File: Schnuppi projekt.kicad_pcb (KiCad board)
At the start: 2 copper layers, 23 parts, among them Q1 BC817, Q2 BC817, SW1 SW_Push, SW2 SW_Push, SW3 SW_Push, SW4 SW_Push, SW5 SW_Push, SW6 SW_Push, U13 ESP32-WROOM-32E, U14 DM-OLED096-636, U2 TPS62065DSGR, U5 WE-TVS-82400102, U6 CH340C

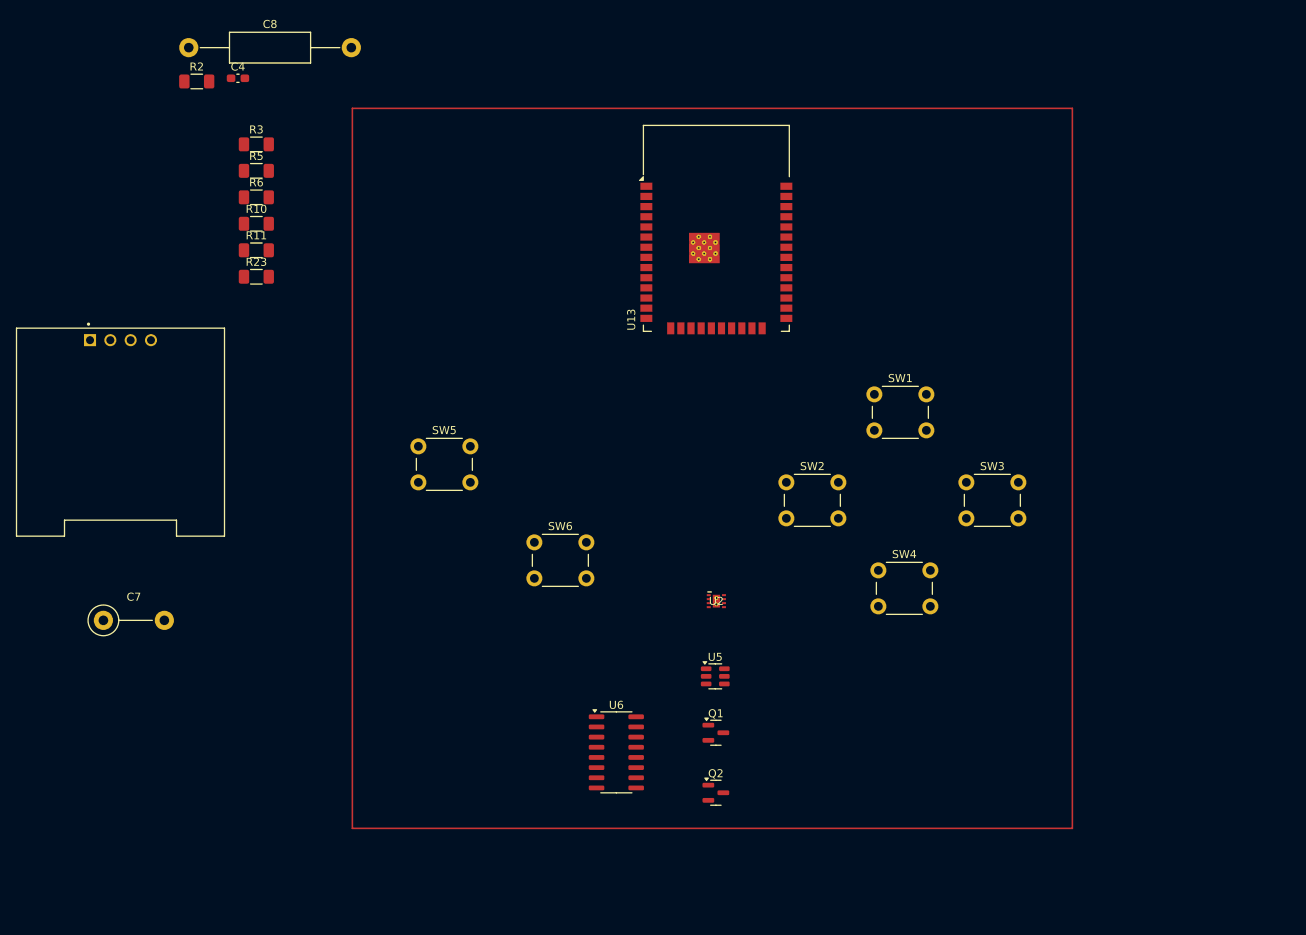
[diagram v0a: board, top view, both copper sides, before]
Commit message: added footprints for resistors
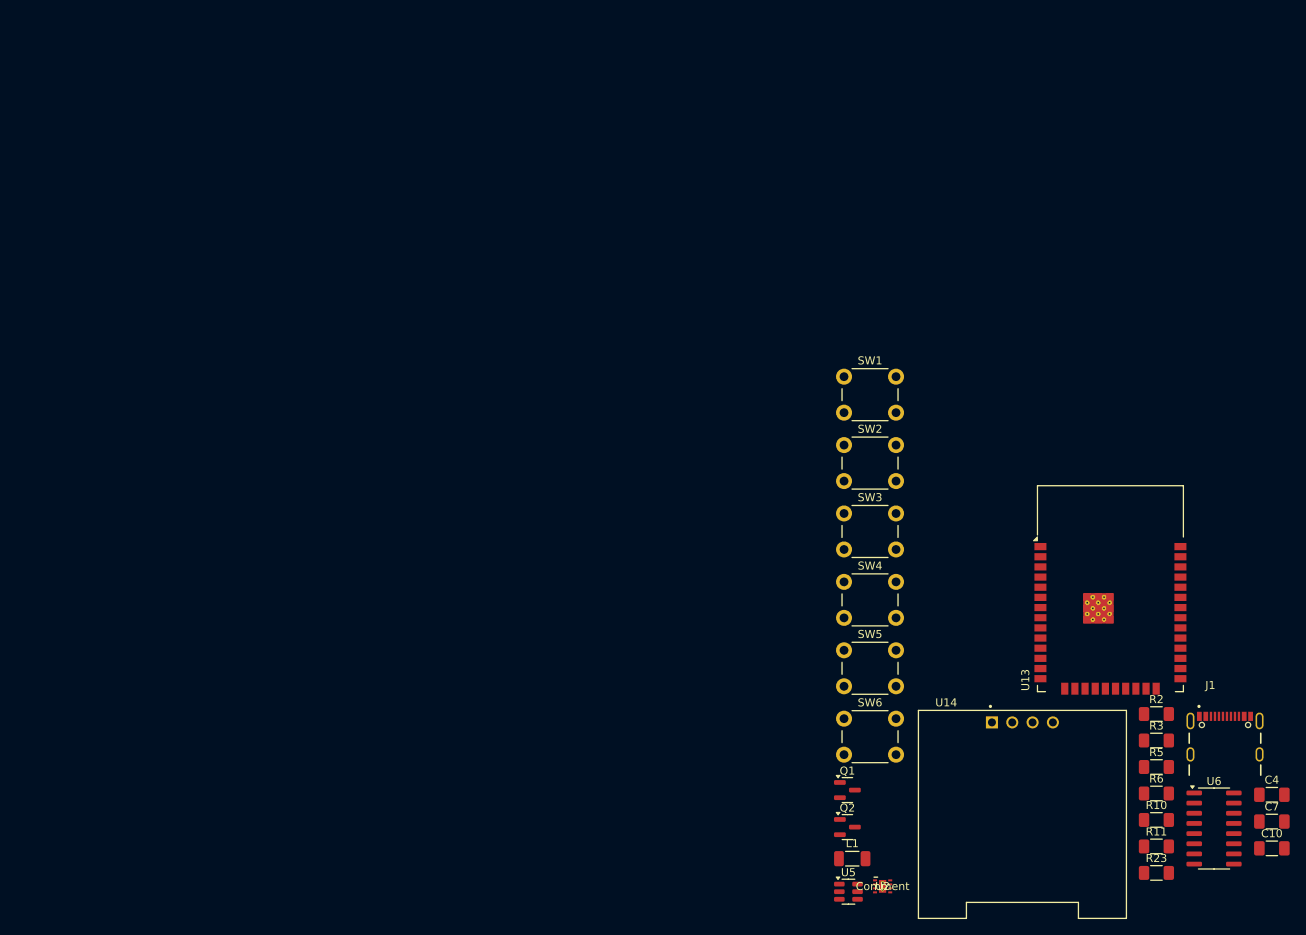
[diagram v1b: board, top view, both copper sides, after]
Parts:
- removed C8: 1uF, Resistor_THT:R_Axial_DIN0411_L9.9mm_D3.6mm_P20.32mm_Horizontal
- added C10: 10uF, Capacitor_SMD:C_1206_3216Metric_Pad1.33x1.80mm_HandSolder, F.Cu at (124.9, 102.5)
- added J1: USB4105-GF-A, USB4105-GF-A (2):GCT_USB4105-GF-A, F.Cu at (119.1, 90.8)
- added L1: 1uH, Inductor_SMD:L_1206_3216Metric_Pad1.22x1.90mm_HandSolder, F.Cu at (72.5, 103.8)
- C4: footprint Capacitor_SMD:C_0603_1608Metric_Pad1.08x0.95mm_HandSolder -> Capacitor_SMD:C_1206_3216Metric_Pad1.33x1.80mm_HandSolder
- C7: footprint Resistor_THT:R_Axial_DIN0411_L9.9mm_D3.6mm_P7.62mm_Vertical -> Capacitor_SMD:C_1206_3216Metric_Pad1.33x1.80mm_HandSolder
- moved C4 157.2 mm to (124.9, 95.8)
- moved C7 148.2 mm to (124.9, 99.2)
- moved R2 143.7 mm to (110.5, 85.7)
- moved R10 134.9 mm to (110.5, 99.0)
- moved R11 134.9 mm to (110.5, 102.3)
- moved R23 134.9 mm to (110.5, 105.6)
- moved R3 134.9 mm to (110.5, 89.0)
- moved R5 134.9 mm to (110.5, 92.3)
- moved R6 134.9 mm to (110.5, 95.6)
- moved U14 122.4 mm to (93.8, 98.3)
- moved U6 75.3 mm to (117.7, 100.0)
- moved U13 66.7 mm to (104.8, 73.0)
- moved SW5 59.0 mm to (71.5, 77.7)
- moved SW6 44.5 mm to (71.5, 86.3)
- moved U2 41.3 mm to (76.3, 107.3)
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
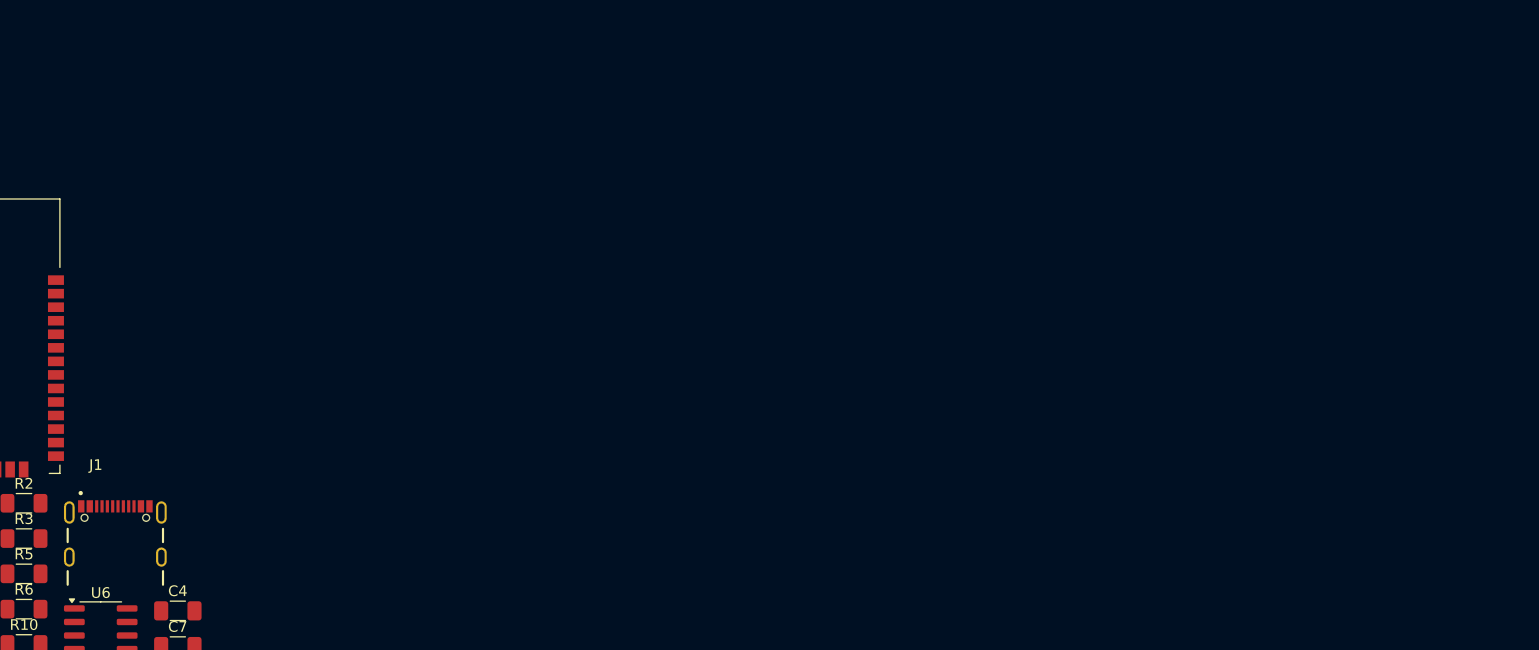
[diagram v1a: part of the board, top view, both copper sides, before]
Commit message: added new footprints
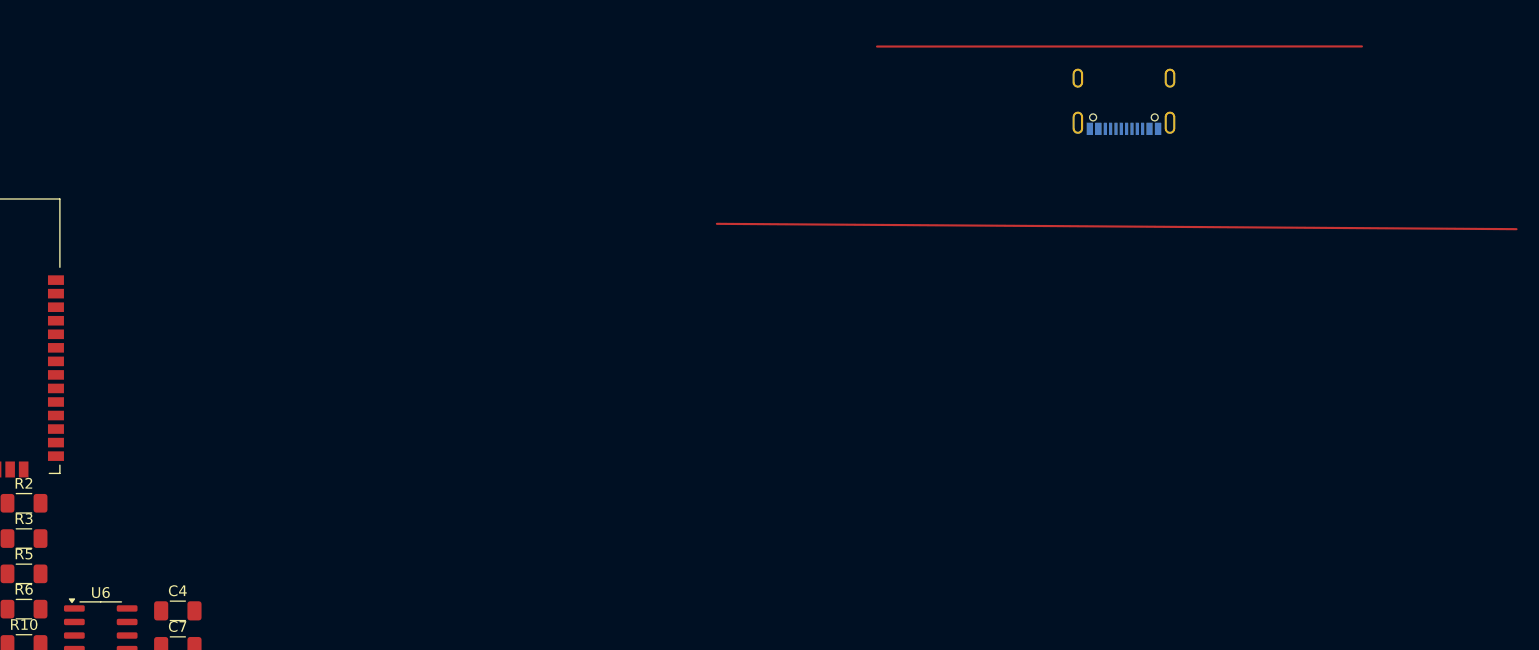
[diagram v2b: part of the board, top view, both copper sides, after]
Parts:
- J1: moved to B.Cu
- moved J1 104.7 mm to (213.7, 45.8)
